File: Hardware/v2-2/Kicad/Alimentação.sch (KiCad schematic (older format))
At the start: 16 parts, among them T1 Module-XFRMR-POE, U16 Ag9200, U17 VIBLSD1-S5-S5-DIP, U18 MEV1D0512DC

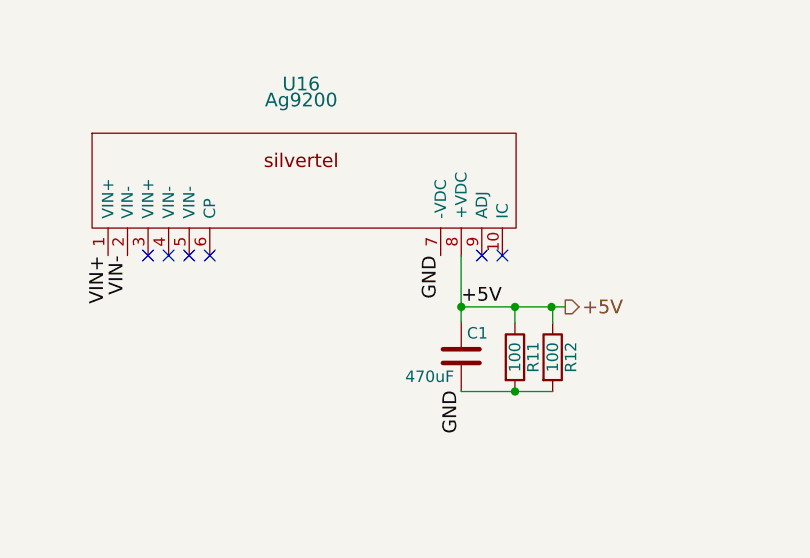
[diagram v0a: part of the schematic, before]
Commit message: New SI and Hardware files - BaseTime via EPICS
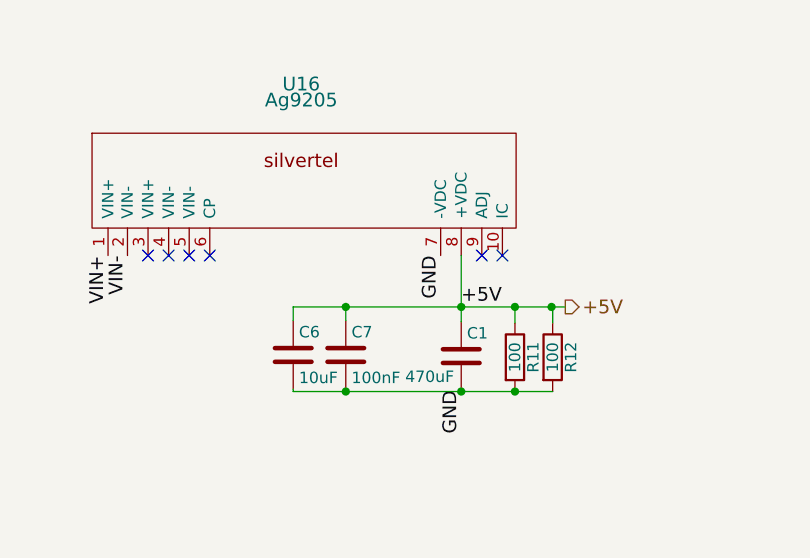
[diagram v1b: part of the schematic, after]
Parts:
- added C6: 10uF, Capacitors_SMD:C_0805, symbol C
- added C7: 100nF, Capacitors_SMD:C_0805, symbol C
- C2, C3, C4: footprint Capacitors_SMD:C_0805_HandSoldering -> Capacitors_SMD:C_0805
- R13, R14, R15, R16: footprint Resistors_SMD:R_0805_HandSoldering -> Resistors_SMD:R_0805
- U16: value Ag9200 -> Ag9205
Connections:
- net +5V: now also C6.1, C7.1
- net GND: now also C6.2, C7.2
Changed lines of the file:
@@
 EESchema Schematic File Version 2
-LIBS:Contador-rescue
 LIBS:power
 LIBS:device
@@
 LIBS:valves
 LIBS:Controle
-LIBS:Contador-cache
+LIBS:CountingPRU_v2-2-cache
 EELAYER 25 0
 EELAYER END
@@
 P 5965 1260
 F 0 "U16" H 5960 1665 60  0000 C CNN
-F 1 "Ag9200" H 5960 1595 60  0000 C CNN
+F 1 "Ag9205" H 5960 1595 60  0000 C CNN
 F 2 "Controle:9200-Silvertel" H 5960 1595 60  0001 C CNN
 F 3 "" H 5960 1595 60  0001 C CNN
@@
 	6660 1895 6660 1605
 Wire Wire Line
-	7060 1900 7060 1830
-Wire Wire Line
-	7060 1830 6660 1830
+	7060 1830 7060 1900
+Wire Wire Line
+	5925 1830 7060 1830
 Connection ~ 6660 1830
 Wire Wire Line
@@
 	6660 2195 6660 2200
 Wire Wire Line
-	6660 2200 7060 2200
+	5925 2200 7060 2200
 Connection ~ 6895 2200
 Text HLabel 7115 1830 2    60   Output ~ 0
@@
 F 0 "C2" H 4640 4450 50  0000 L CNN
 F 1 "4.7uF" H 4640 4250 50  0000 L CNN
-F 2 "Capacitors_SMD:C_0805_HandSoldering" H 4653 4200 50  0001 C CNN
+F 2 "Capacitors_SMD:C_0805" H 4653 4200 50  0001 C CNN
 F 3 "" H 4615 4350 50  0000 C CNN
 	1    4615 4350
@@
 F 0 "C3" H 4050 4745 50  0000 L CNN
 F 1 "1uF" H 4050 4545 50  0000 L CNN
-F 2 "Capacitors_SMD:C_0805_HandSoldering" H 4063 4495 50  0001 C CNN
+F 2 "Capacitors_SMD:C_0805" H 4063 4495 50  0001 C CNN
 F 3 "" H 4025 4645 50  0000 C CNN
 	1    4025 4645
@@
 F 0 "R13" V 4310 4585 50  0000 C CNN
 F 1 "120" V 4230 4585 50  0000 C CNN
-F 2 "Resistors_SMD:R_0805_HandSoldering" V 4160 4585 50  0001 C CNN
+F 2 "Resistors_SMD:R_0805" V 4160 4585 50  0001 C CNN
 F 3 "" H 4230 4585 50  0000 C CNN
 	1    4230 4585
@@
 F 0 "R14" V 4310 4920 50  0000 C CNN
 F 1 "120" V 4230 4920 50  0000 C CNN
-F 2 "Resistors_SMD:R_0805_HandSoldering" V 4160 4920 50  0001 C CNN
+F 2 "Resistors_SMD:R_0805" V 4160 4920 50  0001 C CNN
 F 3 "" H 4230 4920 50  0000 C CNN
 	1    4230 4920
@@
 F 0 "C4" H 5815 4800 50  0000 L CNN
 F 1 "1uF" H 5815 4600 50  0000 L CNN
-F 2 "Capacitors_SMD:C_0805_HandSoldering" H 5828 4550 50  0001 C CNN
+F 2 "Capacitors_SMD:C_0805" H 5828 4550 50  0001 C CNN
 F 3 "" H 5790 4700 50  0000 C CNN
 	1    5790 4700
@@
 F 0 "R15" V 6105 4700 50  0000 C CNN
 F 1 "4.7k" V 6025 4700 50  0000 C CNN
-F 2 "Resistors_SMD:R_0805_HandSoldering" V 5955 4700 50  0001 C CNN
+F 2 "Resistors_SMD:R_0805" V 5955 4700 50  0001 C CNN
 F 3 "" H 6025 4700 50  0000 C CNN
 	1    6025 4700
@@
 F 0 "R16" V 6105 5030 50  0000 C CNN
 F 1 "620" V 6025 5030 50  0000 C CNN
-F 2 "Resistors_SMD:R_0805_HandSoldering" V 5955 5030 50  0001 C CNN
+F 2 "Resistors_SMD:R_0805" V 5955 5030 50  0001 C CNN
 F 3 "" H 6025 5030 50  0000 C CNN
 	1    6025 5030
@@
 NoConn ~ 2900 1465
 NoConn ~ 2900 2410
+$Comp
+L C C7
+U 1 1 5A6F47EC
+P 6155 2040
+F 0 "C7" H 6180 2140 50  0000 L CNN
+F 1 "100nF" H 6180 1940 50  0000 L CNN
+F 2 "Capacitors_SMD:C_0805" H 6193 1890 50  0001 C CNN
+F 3 "" H 6155 2040 50  0000 C CNN
+	1    6155 2040
+	1    0    0    -1
+$EndComp
+$Comp
+L C C6
+U 1 1 5A6F49DD
+P 5925 2040
+F 0 "C6" H 5950 2140 50  0000 L CNN
+F 1 "10uF" H 5950 1940 50  0000 L CNN
+F 2 "Capacitors_SMD:C_0805" H 5963 1890 50  0001 C CNN
+F 3 "" H 5925 2040 50  0000 C CNN
+	1    5925 2040
+	1    0    0    -1
+$EndComp
+Wire Wire Line
+	6155 2200 6155 2190
+Connection ~ 6660 2200
+Wire Wire Line
+	5925 2200 5925 2190
+Connection ~ 6155 2200
+Wire Wire Line
+	6155 1890 6155 1830
+Wire Wire Line
+	5925 1890 5925 1830
+Connection ~ 6155 1830
 $EndSCHEMATC

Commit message: Updating files for 2 LNLS connector
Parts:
- BR1, BR2: value Diode_Bridge -> DF01S-T
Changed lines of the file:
@@
 $Descr A4 11693 8268
 encoding utf-8
-Sheet 2 2
+Sheet 2 4
 Title ""
 Date ""
@@
 P 1300 1230
 F 0 "BR1" H 1050 1530 50  0000 C CNN
-F 1 "Diode_Bridge" H 1650 880 50  0000 C CNN
+F 1 "DF01S-T" H 1650 880 50  0000 C CNN
 F 2 "Controle:RECT_BRIDGE" H 1300 1230 50  0001 C CNN
 F 3 "" H 1300 1230 50  0000 C CNN
@@
 P 1310 2660
 F 0 "BR2" H 1060 2960 50  0000 C CNN
-F 1 "Diode_Bridge" H 1660 2310 50  0000 C CNN
+F 1 "DF01S-T" H 1660 2310 50  0000 C CNN
 F 2 "Controle:RECT_BRIDGE" H 1310 2660 50  0001 C CNN
 F 3 "" H 1310 2660 50  0000 C CNN
